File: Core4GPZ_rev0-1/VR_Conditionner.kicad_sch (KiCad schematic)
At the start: 16 parts, among them IC1 MAX9926UAEE_V+

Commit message: Updated CAD Enclosure STL and STEP export
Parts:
- C5, C6, C7, C8, C9: footprint Capacitor_SMD:C_0805_2012Metric -> Capacitor_SMD:C_0805_2012Metric_Pad1.18x1.45mm_HandSolder
- R10, R7, R8, R9: footprint Resistor_SMD:R_1206_3216Metric -> Resistor_SMD:R_0805_2012Metric_Pad1.20x1.40mm_HandSolder
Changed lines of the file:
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@@
 			)
 		)
-		(property "Footprint" "Capacitor_SMD:C_0805_2012Metric"
+		(property "Footprint" "Capacitor_SMD:C_0805_2012Metric_Pad1.18x1.45mm_HandSolder"
 			(at 148.2852 88.9 0)
 			(effects
@@
 			)
 		)
-		(property "Footprint" "Capacitor_SMD:C_0805_2012Metric"
+		(property "Footprint" "Capacitor_SMD:C_0805_2012Metric_Pad1.18x1.45mm_HandSolder"
 			(at 148.2852 78.74 0)
 			(effects
@@
 			)
 		)
-		(property "Footprint" "Capacitor_SMD:C_0805_2012Metric"
+		(property "Footprint" "Capacitor_SMD:C_0805_2012Metric_Pad1.18x1.45mm_HandSolder"
 			(at 148.2852 99.06 0)
 			(effects
@@
 			)
 		)
-		(property "Footprint" "Resistor_SMD:R_1206_3216Metric"
+		(property "Footprint" "Resistor_SMD:R_0805_2012Metric_Pad1.20x1.40mm_HandSolder"
 			(at 170.18 76.962 90)
 			(effects
@@
 			)
 		)
-		(property "Footprint" "Resistor_SMD:R_1206_3216Metric"
+		(property "Footprint" "Resistor_SMD:R_0805_2012Metric_Pad1.20x1.40mm_HandSolder"
 			(at 170.18 97.282 90)
 			(effects
@@
 			)
 		)
-		(property "Footprint" "Capacitor_SMD:C_0805_2012Metric"
+		(property "Footprint" "Capacitor_SMD:C_0805_2012Metric_Pad1.18x1.45mm_HandSolder"
 			(at 155.9052 88.9 0)
 			(effects
@@
 			)
 		)
-		(property "Footprint" "Resistor_SMD:R_1206_3216Metric"
+		(property "Footprint" "Resistor_SMD:R_0805_2012Metric_Pad1.20x1.40mm_HandSolder"
 			(at 170.18 89.662 90)
 			(effects
@@
 			)
 		)
-		(property "Footprint" "Resistor_SMD:R_1206_3216Metric"
+		(property "Footprint" "Resistor_SMD:R_0805_2012Metric_Pad1.20x1.40mm_HandSolder"
 			(at 170.18 69.342 90)
 			(effects
@@
 			)
 		)
-		(property "Footprint" "Capacitor_SMD:C_0805_2012Metric"
+		(property "Footprint" "Capacitor_SMD:C_0805_2012Metric_Pad1.18x1.45mm_HandSolder"
 			(at 163.5252 88.9 0)
 			(effects

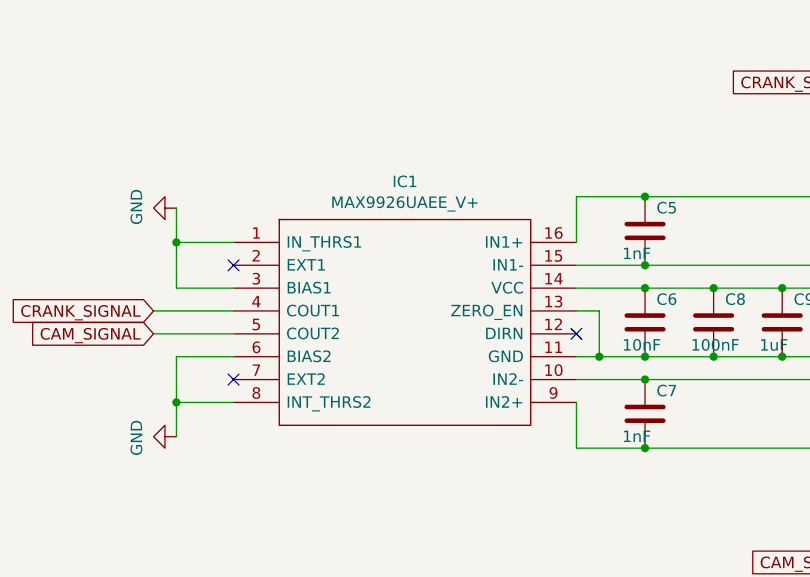
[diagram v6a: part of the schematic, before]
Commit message: Updated component Library with specific parts
Added "Speeduino_bike_prototype" library, with symbols and footprints.
You can add this library to your library table.
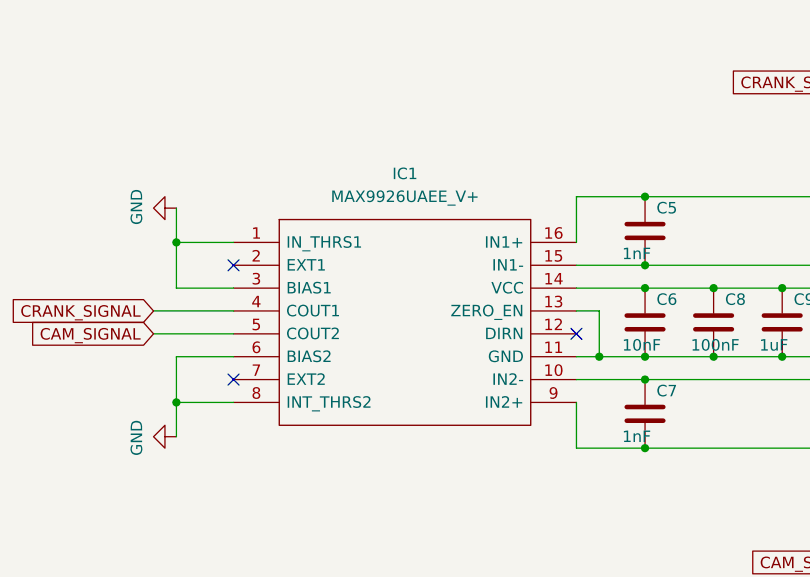
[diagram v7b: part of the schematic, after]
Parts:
- removed IC1: MAX9926UAEE_V+, Package_SO:QSOP-16_3.9x4.9mm_P0.635mm, symbol IC_Automotive:MAX9926UAEE_V+
- added IC1: MAX9926UAEE_V+, Package_SO:QSOP-16_3.9x4.9mm_P0.635mm, symbol Speeduino_Bike_Prototype:MAX9926UAEE_V+
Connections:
- net +5V: now also IC1.14 (VCC)
- net CAM_SIGNAL: now also IC1.5 (COUT2)
- net CRANK_SIGNAL: now also IC1.4 (COUT1)
- net GND: now also IC1.1 (IN_THRS1), IC1.11 (GND), IC1.13 (ZERO_EN), IC1.3 (BIAS1), IC1.6 (BIAS2), IC1.8 (INT_THRS2)
- net at C5.1, R7.2: now also IC1.16 (IN1+)
- net at C5.2, R8.2: now also IC1.15 (IN1-)
- net at C7.1, R9.2: now also IC1.10 (IN2-)
- net at C7.2, R10.2: now also IC1.9 (IN2+)
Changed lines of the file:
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@@
+	)
+	(symbol
+		(lib_id "Speeduino_Bike_Prototype:MAX9926UAEE_V+")
+		(at 120.65 85.09 0)
+		(unit 1)
+		(exclude_from_sim no)
+		(in_bom yes)
+		(on_board yes)
+		(dnp no)
+		(fields_autoplaced yes)
+		(property "Reference" "IC1"
+			(at 120.65 68.58 0)
+			(effects
+				(font
+					(size 1.27 1.27)
+				)
+			)
+		)
+		(property "Value" "MAX9926UAEE_V+"
+			(at 120.65 71.12 0)
+			(effects
+				(font
+					(size 1.27 1.27)
+				)
+			)
+		)
+		(property "Footprint" "Package_SO:QSOP-16_3.9x4.9mm_P0.635mm"
+			(at 106.68 99.06 0)
+			(effects
+				(font
+					(size 1.27 1.27)
+				)
+				(justify left)
+				(hide yes)
+			)
+		)
+		(property "Datasheet" "https://componentsearchengine.com/Datasheets/1/MAX9926UAEE_V+.pdf"
+			(at 106.68 101.6 0)
+			(effects
+				(font
+					(size 1.27 1.27)
+				)
+				(justify left)
+				(hide yes)
+			)
+		)
+		(property "Description" "Sensor Interface Variable-Reluctance Sensor Interface"
+			(at 106.68 104.14 0)
+			(effects
+				(font
+					(size 1.27 1.27)
+				)
+				(justify left)
+				(hide yes)
+			)
+		)
+		(property "Height" "1.75"
+			(at 106.68 106.68 0)
+			(effects
+				(font
+					(size 1.27 1.27)
+				)
+				(justify left)
+				(hide yes)
+			)
+		)
+		(property "Manufacturer_Name" "Maxim Integrated"
+			(at 106.68 109.22 0)
+			(effects
+				(font
+					(size 1.27 1.27)
+				)
+				(justify left)
+				(hide yes)
+			)
+		)
+		(property "Manufacturer_Part_Number" "MAX9926UAEE/V+"
+			(at 106.68 111.76 0)
+			(effects
+				(font
+					(size 1.27 1.27)
+				)
+				(justify left)
+				(hide yes)
+			)
+		)
+		(property "Mouser Part Number" "700-MAX9926UAEE/V+"
+			(at 106.68 114.3 0)
+			(effects
+				(font
+					(size 1.27 1.27)
+				)
+				(justify left)
+				(hide yes)
+			)
+		)
+		(property "Mouser Price/Stock" "https://www.mouser.com/Search/Refine.aspx?Keyword=700-MAX9926UAEE%2FV%2B"
+			(at 106.68 116.84 0)
+			(effects
+				(font
+					(size 1.27 1.27)
+				)
+				(justify left)
+				(hide yes)
+			)
+		)
+		(pin "2"
+		)
+		(pin "5"
+		)
+		(pin "6"
+		)
+		(pin "13"
+		)
+		(pin "14"
+		)
+		(pin "12"
+		)
+		(pin "4"
+		)
+		(pin "9"
+		)
+		(pin "1"
+		)
+		(pin "16"
+		)
+		(pin "11"
+		)
+		(pin "15"
+		)
+		(pin "7"
+		)
+		(pin "8"
+		)
+		(pin "10"
+		)
+		(pin "3"
+		)
+		(instances
+			(project ""
+				(path "/ac28f42d-34b3-4fcc-84dd-ab6106f99610/eddb9d71-e77a-4517-903c-0f4defe5abdd"
+					(reference "IC1")
+					(unit 1)
+				)
+			)
+		)
 	)
 	(symbol
@@
 					(unit 1)
 				)
-			)
-		)
-	)
-	(symbol
-		(lib_id "IC_Automotive:MAX9926UAEE_V+")
-		(at 101.6 76.2 0)
-		(unit 1)
-		(exclude_from_sim no)
-		(in_bom yes)
-		(on_board yes)
-		(dnp no)
-		(property "Reference" "IC1"
-			(at 120.65 69.469 0)
-			(effects
-				(font
-					(size 1.27 1.27)
-				)
-			)
-		)
-		(property "Value" "MAX9926UAEE_V+"
-			(at 120.65 71.7804 0)
-			(effects
-				(font
-					(size 1.27 1.27)
-				)
-			)
-		)
-		(property "Footprint" "Package_SO:QSOP-16_3.9x4.9mm_P0.635mm"
-			(at 135.89 73.66 0)
-			(effects
-				(font
-					(size 1.27 1.27)
-				)
-				(justify left)
-				(hide yes)
-			)
-		)
-		(property "Datasheet" "https://componentsearchengine.com/Datasheets/1/MAX9926UAEE_V+.pdf"
-			(at 135.89 76.2 0)
-			(effects
-				(font
-					(size 1.27 1.27)
-				)
-				(justify left)
-				(hide yes)
-			)
-		)
-		(property "Description" "Sensor Interface Variable-Reluctance Sensor Interface"
-			(at 135.89 78.74 0)
-			(effects
-				(font
-					(size 1.27 1.27)
-				)
-				(justify left)
-				(hide yes)
-			)
-		)
-		(property "Height" "1.75"
-			(at 135.89 81.28 0)
-			(effects
-				(font
-					(size 1.27 1.27)
-				)
-				(justify left)
-				(hide yes)
-			)
-		)
-		(property "Manufacturer_Name" "Maxim Integrated"
-			(at 135.89 83.82 0)
-			(effects
-				(font
-					(size 1.27 1.27)
-				)
-				(justify left)
-				(hide yes)
-			)
-		)
-		(property "Manufacturer_Part_Number" "MAX9926UAEE/V+"
-			(at 135.89 86.36 0)
-			(effects
-				(font
-					(size 1.27 1.27)
-				)
-				(justify left)
-				(hide yes)
-			)
-		)
-		(property "Mouser Part Number" "700-MAX9926UAEE/V+"
-			(at 135.89 88.9 0)
-			(effects
-				(font
-					(size 1.27 1.27)
-				)
-				(justify left)
-				(hide yes)
-			)
-		)
-		(property "Mouser Price/Stock" "https://www.mouser.com/Search/Refine.aspx?Keyword=700-MAX9926UAEE%2FV%2B"
-			(at 135.89 91.44 0)
-			(effects
-				(font
-					(size 1.27 1.27)
-				)
-				(justify left)
-				(hide yes)
-			)
-		)
-		(property "Digikey Part Number" "MAX9926UAEE/V+-ND"
-			(at 101.6 76.2 0)
-			(effects
-				(font
-					(size 1.27 1.27)
-				)
-				(hide yes)
-			)
-		)
-		(property "URL" "https://www.digikey.com.au/product-detail/en/maxim-integrated/MAX9926UAEE-V/MAX9926UAEE-V-ND/3517309"
-			(at 101.6 76.2 0)
-			(effects
-				(font
-					(size 1.27 1.27)
-				)
-				(hide yes)
-			)
-		)
-		(pin "1"
-		)
-		(pin "10"
-		)
-		(pin "11"
-		)
-		(pin "12"
-		)
-		(pin "13"
-		)
-		(pin "14"
-		)
-		(pin "15"
-		)
-		(pin "16"
-		)
-		(pin "2"
-		)
-		(pin "3"
-		)
-		(pin "4"
-		)
-		(pin "5"
-		)
-		(pin "6"
-		)
-		(pin "7"
-		)
-		(pin "8"
-		)
-		(pin "9"
-		)
-		(instances
-			(project "Core4GPZ_rev0-1"
-				(path "/ac28f42d-34b3-4fcc-84dd-ab6106f99610/eddb9d71-e77a-4517-903c-0f4defe5abdd"
-					(reference "IC1")
-					(unit 1)
-				)

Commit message: Updated project library, BOM and documentation
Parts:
- removed C7: 1nF, Capacitor_SMD:C_0805_2012Metric_Pad1.18x1.45mm_HandSolder, symbol Device:C
- removed IC1: MAX9926UAEE_V+, Package_SO:QSOP-16_3.9x4.9mm_P0.635mm, symbol Speeduino_Bike_Prototype:MAX9926UAEE_V+
- removed R8, R9: 10k, Resistor_SMD:R_0805_2012Metric_Pad1.20x1.40mm_HandSolder, symbol Device:R
- added C6: 1nF, Capacitor_SMD:C_0805_2012Metric_Pad1.18x1.45mm_HandSolder, symbol Device:C
- added IC1: MAX9926UAEE_V+, Package_SO:QSOP-16_3.9x4.9mm_P0.635mm, symbol Bike_Prototype_LIB:MAX9926UAEE_V+
- added R11, R12: 10k, Resistor_SMD:R_1206_3216Metric_Pad1.30x1.75mm_HandSolder, symbol Device:R
- C4: renamed from C5; Mouser (none) -> https://www.mouser.fr/ProductDetail/KEMET/C0805C102J5HACAUTO
- C5: renamed from C6; Mouser (none) -> https://www.mouser.fr/ProductDetail/YAGEO/CC0805KRX7R9BB103
- C7: renamed from C8; Mouser (none) -> https://www.mouser.fr/ProductDetail/YAGEO/CC0805KRX7R9BB104
- R10: footprint Resistor_SMD:R_0805_2012Metric_Pad1.20x1.40mm_HandSolder -> Resistor_SMD:R_1206_3216Metric_Pad1.30x1.75mm_HandSolder
- R13, R14: Manufacturer (none) -> Yageo; Manufacturer_part (none) -> RC0805FR-071KL; Mouser (none) -> https://www.mouser.fr/ProductDetail/YAGEO/RC0805FR-071KL?qs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
- R9: renamed from R7; footprint Resistor_SMD:R_0805_2012Metric_Pad1.20x1.40mm_HandSolder -> Resistor_SMD:R_1206_3216Metric_Pad1.30x1.75mm_HandSolder
- renumbered C9 to C8, JP3 to JP5, JP4 to JP6
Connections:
- net +5V: now also IC1.14 (VCC)
- net CAM_SIGNAL: now also IC1.5 (COUT2)
- net CAM_SNSR_VR-: now also R11.1
- net CRANK_SIGNAL: now also IC1.4 (COUT1)
- net CRANK_SNSR_VR-: now also R10.1
- net GND: now also IC1.1 (IN_THRS1), IC1.11 (GND), IC1.13 (ZERO_EN), IC1.3 (BIAS1), IC1.6 (BIAS2), IC1.8 (INT_THRS2)
- net at C4.1, R9.2: now also IC1.16 (IN1+)
- net at C4.2: now also R10.2, IC1.15 (IN1-)
- net at JP6.3 (B): now also R12.1; no longer R10.1
- new net: C6.1, IC1.10 (IN2-), R11.2
- new net: C6.2, IC1.9 (IN2+), R12.2
